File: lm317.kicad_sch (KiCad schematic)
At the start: 18 parts, among them T1 Transformer_1P_1S, U15 LM317L_SOT-89, U16 LM317L_SOT-89

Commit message: Chip decided
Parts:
- added 2W,5.1Ohm8: R, Resistor_THT:R_Axial_DIN0414_L11.9mm_D4.5mm_P15.24mm_Horizontal, symbol Device:R
- added C22, C23: 22qf, Capacitor_THT:CP_Radial_D5.0mm_P2.00mm, symbol Device:C
- added U20: BQ7790500PWR, PW20_TEX, symbol BQ77905:BQ7790500PWR
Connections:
- net GND: now also 2W,5.1Ohm8.2, C22.1, C23.1
- new net: 2W,5.1Ohm8.1, C23.2
- new net: C22.2, U20.2 (AVDD)

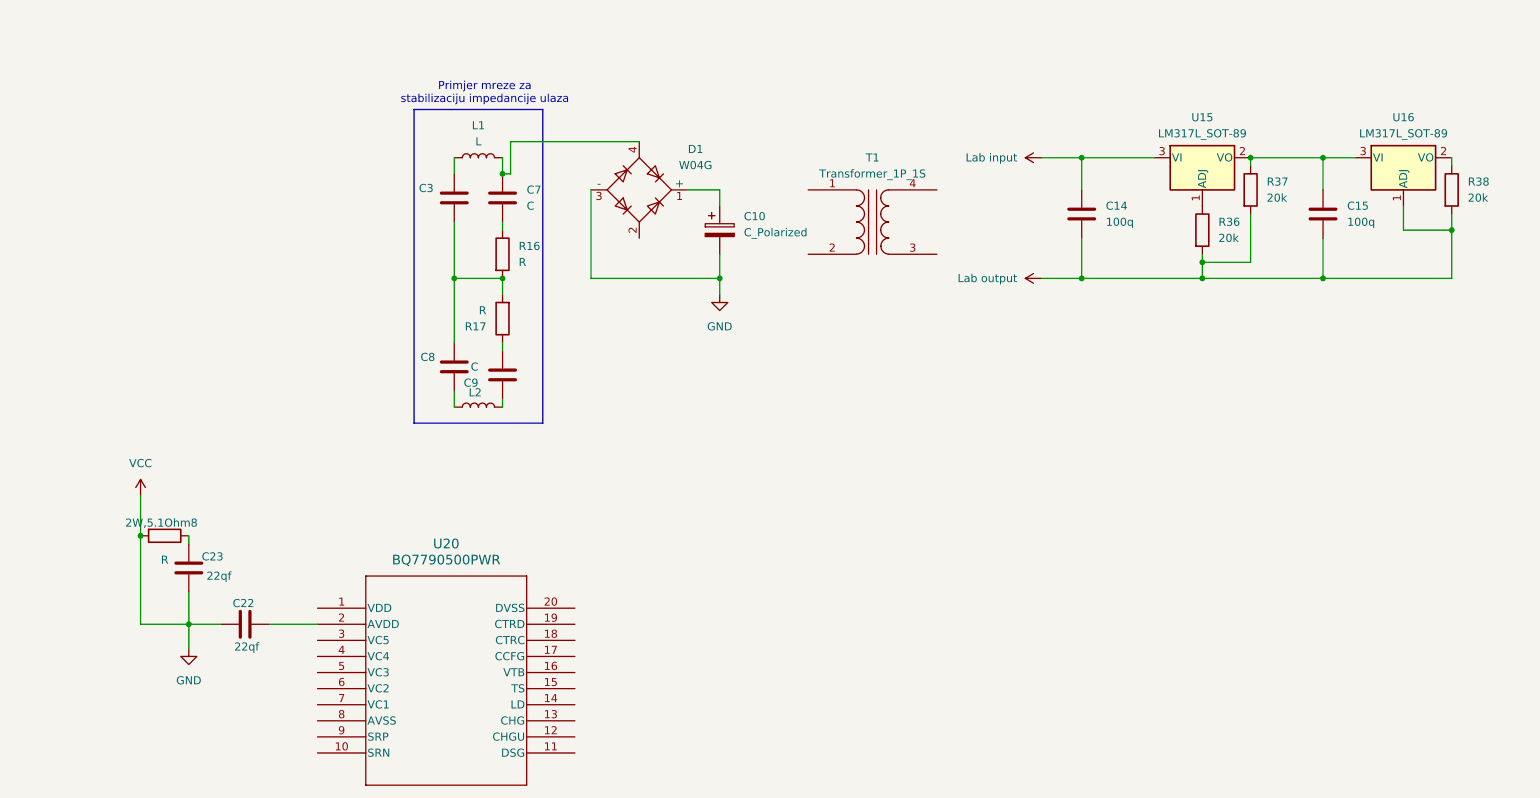
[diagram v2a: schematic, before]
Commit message: flyback transformer
Flyback transformer fixed along with regulation
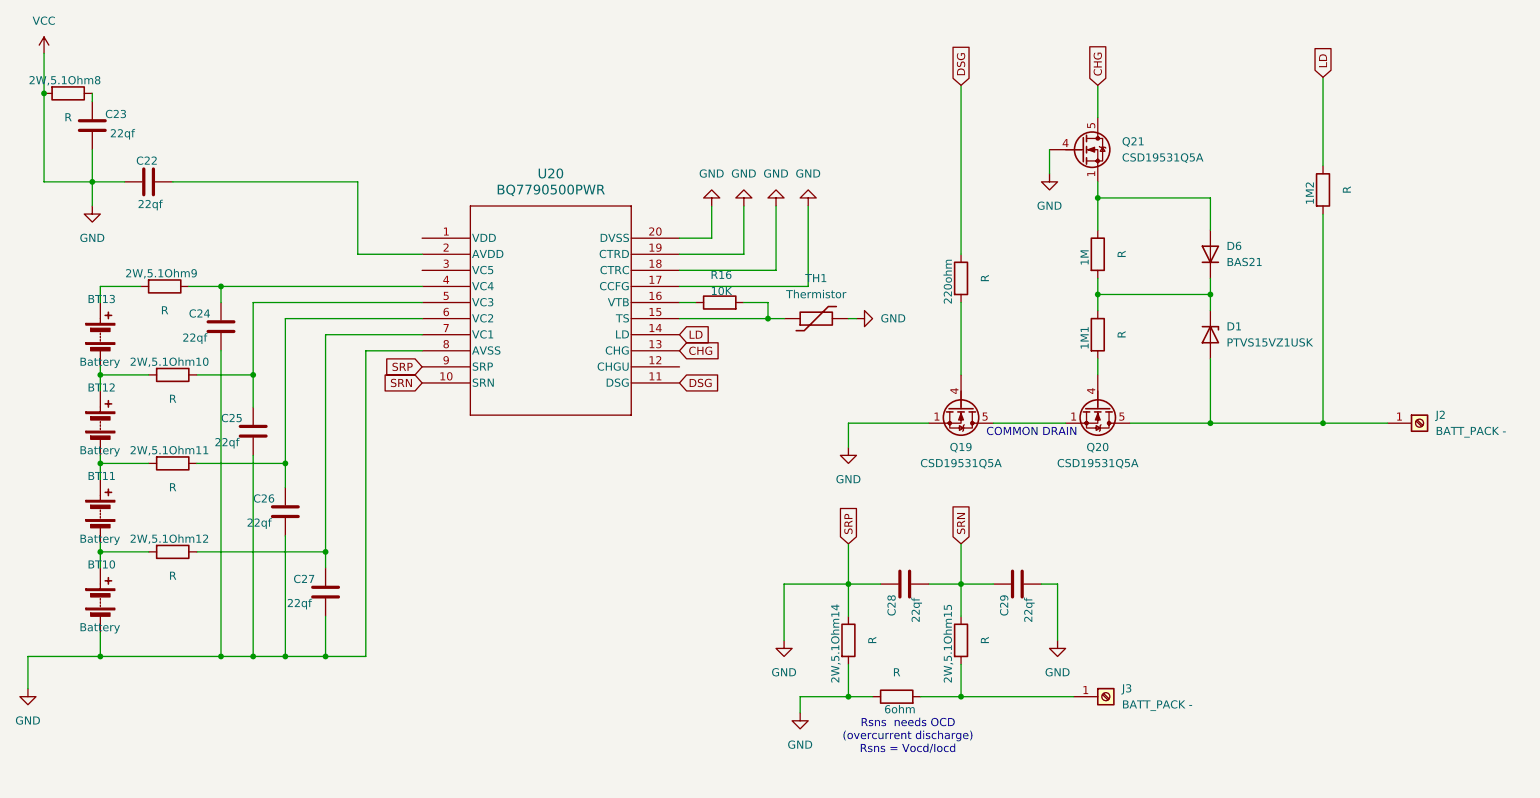
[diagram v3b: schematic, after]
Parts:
- removed C10: C_Polarized, symbol Device:C_Polarized
- removed C14, C15: 100q, Capacitor_SMD:C_0805_2012Metric, symbol Device:C
- removed C3, C7, C8, C9: C, symbol Device:C
- removed D1: W04G, Diode_THT:Diode_Bridge_Round_D9.8mm, symbol Diode_Bridge:W04G
- removed L1, L2: L, symbol Device:L
- removed R17: R, symbol Device:R
- removed R36, R37, R38: 20k, Resistor_SMD:R_0805_2012Metric, symbol Device:R
- removed T1: Transformer_1P_1S, symbol Device:Transformer_1P_1S
- removed U15, U16: LM317L_SOT-89, Package_TO_SOT_SMD:SOT-89-3, symbol Regulator_Linear:LM317L_SOT-89
- added 1M, 1M1, 1M2, 220ohm, 2W,5.1Ohm10, 2W,5.1Ohm11, 2W,5.1Ohm12, 2W,5.1Ohm14, 2W,5.1Ohm15, 2W,5.1Ohm9, 6ohm: R, Resistor_THT:R_Axial_DIN0414_L11.9mm_D4.5mm_P15.24mm_Horizontal, symbol Device:R
- added BT10, BT11, BT12, BT13: Battery, symbol Device:Battery
- added C24, C25, C26, C27, C28, C29: 22qf, Capacitor_THT:CP_Radial_D5.0mm_P2.00mm, symbol Device:C
- added D1: PTVS15VZ1USK, Diode_SMD:Nexperia_DSN1608-2_1.6x0.8mm, symbol Diode:PTVS15VZ1USK
- added D6: BAS21, Package_TO_SOT_SMD:SOT-23, symbol Diode:BAS21
- added J2, J3: BATT_PACK -, symbol Connector:Screw_Terminal_01x01
- added Q19, Q20, Q21: CSD19531Q5A, Package_TO_SOT_SMD:TDSON-8-1, symbol Transistor_FET:CSD19531Q5A
- added TH1: Thermistor, symbol Device:Thermistor
- R16: value R -> 10K; footprint (none) -> Resistor_SMD:R_0805_2012Metric
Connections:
- net GND: now also U20.17 (CCFG), U20.18 (CTRC), U20.19 (CTRD), U20.20 (DVSS), U20.8 (AVSS), U20.9 (SRP), 2W,5.1Ohm14.1, 2W,5.1Ohm14.2, 6ohm.1, BT10.2 (-), C24.1, C25.1, C26.1, C27.1, C28.2, C29.1, Q19.1 (S), Q19.2 (S), Q19.3 (S), Q21.4 (G), TH1.2
- net at R16.1: now also U20.16 (VTB)
- net at R16.2: now also U20.15 (TS), TH1.1
- net SRN: now reaches U20.10 (SRN)
- net SRN: now also 2W,5.1Ohm15.1, C28.1, C29.2
- net DSG: now reaches U20.11 (DSG)
- net DSG: now also 220ohm.1
- net CHG: now reaches U20.13 (CHG)
- net CHG: now also Q21.5 (D)
- net LD: now reaches U20.14 (LD)
- net LD: now also 1M2.1
- net at U20.4 (VC4): now also 2W,5.1Ohm9.1, C24.2
- net at U20.5 (VC3): now also 2W,5.1Ohm10.1, C25.2
- net at U20.6 (VC2): now also 2W,5.1Ohm11.1, C26.2
- net at U20.7 (VC1): now also 2W,5.1Ohm12.1, C27.2
- new net: 2W,5.1Ohm12.2, BT10.1 (+), BT11.2 (-)
- new net: 1M.1, D6.1 (A), Q21.1 (S), Q21.2 (S), Q21.3 (S)
- new net: 1M.2, 1M1.1, D1.1 (K), D6.3 (K)
- new net: 1M1.2, Q20.4 (G)
- new net: 2W,5.1Ohm10.2, BT12.1 (+), BT13.2 (-)
- new net: 1M2.2, D1.2 (A), J2.1 (Pin_1), Q20.5 (D)
- new net: 2W,5.1Ohm15.2, 6ohm.2, J3.1 (Pin_1)
- new net: 220ohm.2, Q19.4 (G)
- new net: Q19.5 (D), Q20.1 (S), Q20.2 (S), Q20.3 (S)
- new net: 2W,5.1Ohm11.2, BT11.1 (+), BT12.2 (-)
- new net: 2W,5.1Ohm9.2, BT13.1 (+)
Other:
- note added: "COMMON DRAIN"
- note added: "Rsns needs OCD (overcurrent discharge) Rsns = Vocd/Iocd"
- note removed: "Primjer mreze za stabilizaciju impedancije ulaza"
- moved on the sheet: 2W,5.1Ohm8, C22, C23, U20
